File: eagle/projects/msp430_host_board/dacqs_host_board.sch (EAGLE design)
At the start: 167 parts, among them J1 MOL-SL-4-RA, J10 MOL-SL-3-V, J13 JST-PH-2TH-RA, J14 USB_MICROB_RECPT, J16 MOL-SL-2-RA, J17 CLM-112-02-L-D-IMU-MOUNT_IMU, J18 MOLSL-7-RA, J2 MOL-SL-4-RA, J3 MOL-SL-4-RA, J4 MOL-SL-4-RA, J5 MOL-SL-5-RA, J6 MOL-SL-3-V, J7 MOL-SL-5-V, J8 MOL-SL-3-RA, J9 MOL-SL-4-RA, U1 MSP430FR4994, U10 LSM9DS1, U2 MSP430FR4994, U3 PCT2075D,118, U4 MS560702BA03-50, U5 TPS61240DRVR, U6 LP5907_DBV_5, U7 MCP73831T, U8 INA219AIDCNR, U9 STD12NF06LT4, Y1 32.768kHz, Y2 4MHz, Y3 32.768kHz, Y4 4MHz

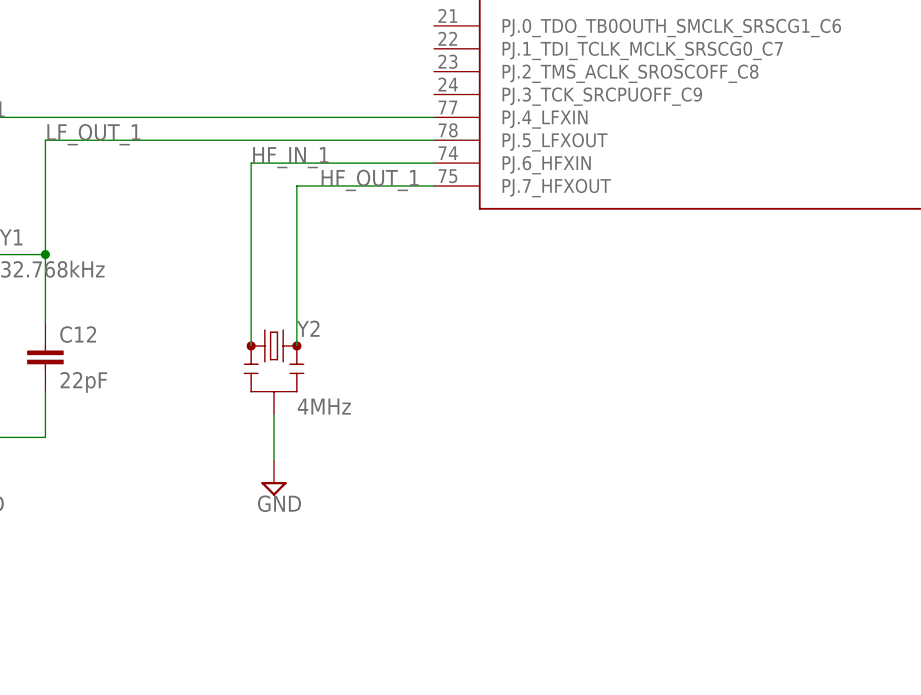
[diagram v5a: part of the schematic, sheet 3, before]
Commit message: Added 24Mhz oscillator for MSP430s
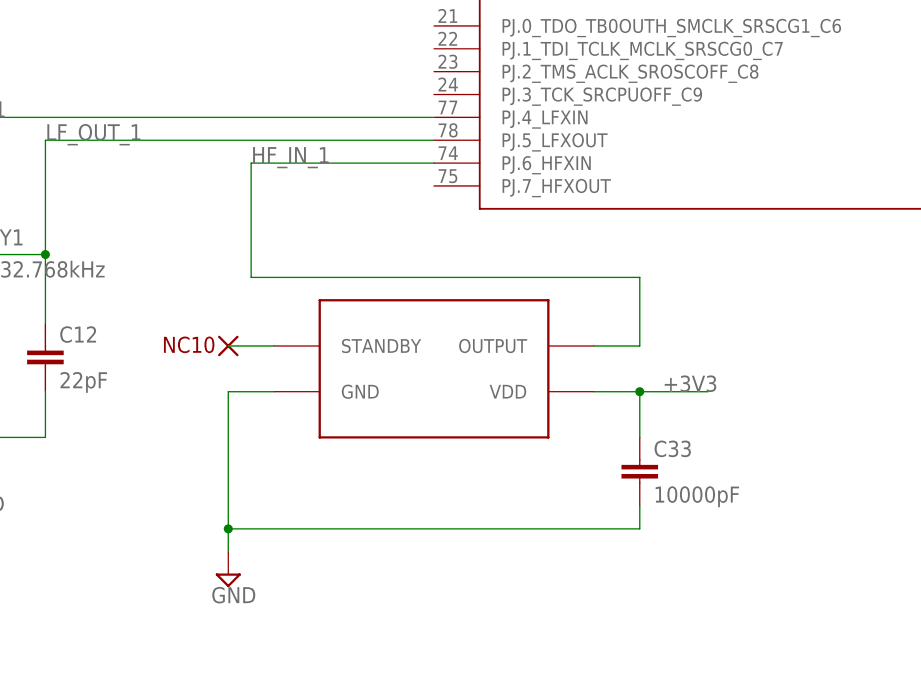
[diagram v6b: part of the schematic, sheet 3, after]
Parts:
- removed Y2, Y4: 4MHz, daqcs_host:RESONATOR4MHZ
- added C33, C34: 10000pF, daqcs_host:CAP_10000PF0_0603
- added NC10, NC11: NC, daqcs_host:NO_CONNECT
- added U$4, U$5: ASEMB-24MHZ-XY-T, daqcs_host:ASEMB-24MHZ-XY-T
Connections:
- removed net HF_OUT_1: U1.PJ.7_HFXOUT, Y2.3
- removed net HF_OUT_2: U2.PJ.7_HFXOUT, Y4.3
- new net N$4: NC10.NC, U$4.STANDBY
- new net N$5: NC11.NC, U$5.STANDBY
- net +3V3: now also C33.1, C34.1, U$4.VDD, U$5.VDD
- net GND: now also C33.2, C34.2, U$4.GND, U$5.GND; no longer Y2.2, Y4.2
- net HF_IN_1: now also U$4.OUTPUT; no longer Y2.1
- net HF_IN_2: now also U$5.OUTPUT; no longer Y4.1
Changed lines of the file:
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@@
 <part name="SUPPLY2" library="supply2" deviceset="GND" device=""/>
 <part name="Y1" library="daqcs_host" deviceset="CRYSTAL" device="3.2X1.5MM" value="32.768kHz"/>
-<part name="Y2" library="daqcs_host" deviceset="RESONATOR" device="4MHZ" value="4MHz"/>
 <part name="C11" library="daqcs_host" deviceset="CAP" device="_0603" technology="_22PF0" value="22pF"/>
 <part name="C12" library="daqcs_host" deviceset="CAP" device="_0603" technology="_22PF0" value="22pF"/>
@@
 <part name="SUPPLY4" library="supply2" deviceset="GND" device=""/>
 <part name="Y3" library="daqcs_host" deviceset="CRYSTAL" device="3.2X1.5MM" value="32.768kHz"/>
-<part name="Y4" library="daqcs_host" deviceset="RESONATOR" device="4MHZ" value="4MHz"/>
 <part name="C13" library="daqcs_host" deviceset="CAP" device="_0603" technology="_22PF0" value="22pF"/>
 <part name="C14" library="daqcs_host" deviceset="CAP" device="_0603" technology="_22PF0" value="22pF"/>
@@
 <part name="TP38" library="daqcs_host" deviceset="TEST_POINT" device="_10R_SMD" technology="_TP10R_SMD"/>
 <part name="U9" library="daqcs_host" deviceset="STD12NF06LT4" device=""/>
+<part name="U$4" library="daqcs_host" deviceset="ASEMB-24MHZ-XY-T" device=""/>
+<part name="NC10" library="daqcs_host" deviceset="NO_CONNECT" device="" value="NC"/>
+<part name="C33" library="daqcs_host" deviceset="CAP" device="_0603" technology="_10000PF0" value="10000pF"/>
+<part name="U$5" library="daqcs_host" deviceset="ASEMB-24MHZ-XY-T" device=""/>
+<part name="NC11" library="daqcs_host" deviceset="NO_CONNECT" device="" value="NC"/>
+<part name="C34" library="daqcs_host" deviceset="CAP" device="_0603" technology="_10000PF0" value="10000pF"/>
 </parts>
 <sheets>
@@
 <instance part="SUPPLY1" gate="GND" x="251.46" y="55.88"/>
 <instance part="Y1" gate="G$1" x="5.08" y="55.88"/>
-<instance part="Y2" gate="G$1" x="38.1" y="45.72"/>
 <instance part="C11" gate="G$1" x="-2.54" y="43.18"/>
 <instance part="C12" gate="G$1" x="12.7" y="43.18"/>
 <instance part="SUPPLY3" gate="GND" x="5.08" y="30.48"/>
-<instance part="SUPPLY4" gate="GND" x="38.1" y="30.48"/>
+<instance part="SUPPLY4" gate="GND" x="33.02" y="20.32"/>
 <instance part="DS4" gate="G$1" x="-15.24" y="172.72" rot="R270"/>
 <instance part="DS5" gate="G$1" x="-15.24" y="160.02" rot="R270"/>
@@
 <instance part="R27" gate="G$1" x="7.62" y="160.02"/>
 <instance part="SUPPLY31" gate="GND" x="-25.4" y="149.86"/>
+<instance part="U$4" gate="G$1" x="55.88" y="43.18"/>
+<instance part="NC10" gate="G$1" x="33.02" y="45.72"/>
+<instance part="C33" gate="G$1" x="78.74" y="30.48"/>
 </instances>
 <busses>
@@
 <junction x="271.78" y="78.74"/>
 <pinref part="+3V2" gate="G$1" pin="+3V3"/>
+</segment>
+<segment>
+<pinref part="U$4" gate="G$1" pin="VDD"/>
+<wire x1="73.66" y1="40.64" x2="78.74" y2="40.64" width="0.1524" layer="91"/>
+<label x="81.28" y="40.64" size="1.778" layer="95"/>
+<pinref part="C33" gate="G$1" pin="1"/>
+<wire x1="78.74" y1="40.64" x2="86.36" y2="40.64" width="0.1524" layer="91"/>
+<wire x1="78.74" y1="40.64" x2="78.74" y2="35.56" width="0.1524" layer="91"/>
+<junction x="78.74" y="40.64"/>
 </segment>
 </net>
@@
 </segment>
 <segment>
-<pinref part="Y2" gate="G$1" pin="2"/>
 <pinref part="SUPPLY4" gate="GND" pin="GND"/>
-<wire x1="38.1" y1="38.1" x2="38.1" y2="33.02" width="0.1524" layer="91"/>
+<wire x1="33.02" y1="40.64" x2="33.02" y2="25.4" width="0.1524" layer="91"/>
+<pinref part="U$4" gate="G$1" pin="GND"/>
+<wire x1="33.02" y1="25.4" x2="33.02" y2="22.86" width="0.1524" layer="91"/>
+<wire x1="38.1" y1="40.64" x2="33.02" y2="40.64" width="0.1524" layer="91"/>
+<pinref part="C33" gate="G$1" pin="2"/>
+<wire x1="78.74" y1="27.94" x2="78.74" y2="25.4" width="0.1524" layer="91"/>
+<wire x1="78.74" y1="25.4" x2="33.02" y2="25.4" width="0.1524" layer="91"/>
+<junction x="33.02" y="25.4"/>
 </segment>
 <segment>
@@
 </segment>
 </net>
-<net name="HF_OUT_1" class="0">
-<segment>
-<pinref part="U1" gate="A" pin="PJ.7_HFXOUT"/>
-<pinref part="Y2" gate="G$1" pin="3"/>
-<wire x1="55.88" y1="63.5" x2="40.64" y2="63.5" width="0.1524" layer="91"/>
-<wire x1="40.64" y1="63.5" x2="40.64" y2="45.72" width="0.1524" layer="91"/>
-<label x="43.18" y="63.5" size="1.778" layer="95"/>
-</segment>
-</net>
 <net name="HF_IN_1" class="0">
 <segment>
-<pinref part="Y2" gate="G$1" pin="1"/>
-<wire x1="35.56" y1="45.72" x2="35.56" y2="66.04" width="0.1524" layer="91"/>
 <pinref part="U1" gate="A" pin="PJ.6_HFXIN"/>
 <wire x1="35.56" y1="66.04" x2="55.88" y2="66.04" width="0.1524" layer="91"/>
 <label x="35.56" y="66.04" size="1.778" layer="95"/>
+<pinref part="U$4" gate="G$1" pin="OUTPUT"/>
+<wire x1="73.66" y1="45.72" x2="78.74" y2="45.72" width="0.1524" layer="91"/>
+<wire x1="78.74" y1="45.72" x2="78.74" y2="53.34" width="0.1524" layer="91"/>
+<wire x1="78.74" y1="53.34" x2="35.56" y2="53.34" width="0.1524" layer="91"/>
+<wire x1="35.56" y1="53.34" x2="35.56" y2="66.04" width="0.1524" layer="91"/>
 </segment>
 </net>
@@
 <wire x1="2.54" y1="172.72" x2="-12.7" y2="172.72" width="0.1524" layer="91"/>
 <label x="-12.7" y="172.72" size="1.778" layer="95"/>
+</segment>
+</net>
+<net name="N$4" class="0">
+<segment>
+<pinref part="NC10" gate="G$1" pin="NC"/>
+<pinref part="U$4" gate="G$1" pin="STANDBY"/>
+<wire x1="33.02" y1="45.72" x2="38.1" y2="45.72" width="0.1524" layer="91"/>
 </segment>
 </net>
@@
 <instance part="SUPPLY2" gate="GND" x="289.56" y="60.96"/>
 <instance part="Y3" gate="G$1" x="40.64" y="58.42"/>
-<instance part="Y4" gate="G$1" x="76.2" y="50.8"/>
 <instance part="C13" gate="G$1" x="33.02" y="45.72"/>
 <instance part="C14" gate="G$1" x="50.8" y="45.72"/>
 <instance part="SUPPLY5" gate="GND" x="40.64" y="33.02"/>
-<instance part="SUPPLY6" gate="GND" x="76.2" y="33.02"/>
+<instance part="SUPPLY6" gate="GND" x="73.66" y="25.4"/>
 <instance part="R4" gate="G$1" x="-12.7" y="175.26" smashed="yes" rot="R90">
 <attribute name="NAME" x="-14.1986" y="176.53" size="1.778" layer="95" rot="R180"/>
@@
 </instance>
 <instance part="DS7" gate="G$1" x="20.32" y="170.18" rot="R270"/>
+<instance part="U$5" gate="G$1" x="96.52" y="48.26"/>
+<instance part="NC11" gate="G$1" x="73.66" y="50.8"/>
+<instance part="C34" gate="G$1" x="116.84" y="38.1"/>
 </instances>
 <busses>
@@
 <wire x1="40.64" y1="149.86" x2="40.64" y2="147.32" width="0.1524" layer="91"/>
 <junction x="33.02" y="149.86"/>
+</segment>
+<segment>
+<pinref part="U$5" gate="G$1" pin="VDD"/>
+<wire x1="114.3" y1="45.72" x2="116.84" y2="45.72" width="0.1524" layer="91"/>
+<pinref part="C34" gate="G$1" pin="1"/>
+<wire x1="116.84" y1="45.72" x2="129.54" y2="45.72" width="0.1524" layer="91"/>
+<wire x1="116.84" y1="45.72" x2="116.84" y2="43.18" width="0.1524" layer="91"/>
+<junction x="116.84" y="45.72"/>
+<label x="121.92" y="45.72" size="1.778" layer="95"/>
 </segment>
 </net>
@@
 </segment>
 <segment>
-<pinref part="Y4" gate="G$1" pin="2"/>
 <pinref part="SUPPLY6" gate="GND" pin="GND"/>
-<wire x1="76.2" y1="43.18" x2="76.2" y2="35.56" width="0.1524" layer="91"/>
+<wire x1="73.66" y1="45.72" x2="73.66" y2="33.02" width="0.1524" layer="91"/>
+<pinref part="U$5" gate="G$1" pin="GND"/>
+<wire x1="73.66" y1="33.02" x2="73.66" y2="27.94" width="0.1524" layer="91"/>
+<wire x1="78.74" y1="45.72" x2="73.66" y2="45.72" width="0.1524" layer="91"/>
+<pinref part="C34" gate="G$1" pin="2"/>
+<wire x1="116.84" y1="35.56" x2="116.84" y2="33.02" width="0.1524" layer="91"/>
+<wire x1="116.84" y1="33.02" x2="73.66" y2="33.02" width="0.1524" layer="91"/>
+<junction x="73.66" y="33.02"/>
 </segment>
 <segment>
@@
 <net name="HF_IN_2" class="0">
 <segment>
-<pinref part="Y4" gate="G$1" pin="1"/>
-<wire x1="73.66" y1="50.8" x2="73.66" y2="71.12" width="0.1524" layer="91"/>
 <pinref part="U2" gate="A" pin="PJ.6_HFXIN"/>
 <wire x1="73.66" y1="71.12" x2="91.44" y2="71.12" width="0.1524" layer="91"/>
 <label x="73.66" y="71.12" size="1.778" layer="95"/>
-</segment>
-</net>
-<net name="HF_OUT_2" class="0">
-<segment>
-<pinref part="U2" gate="A" pin="PJ.7_HFXOUT"/>
-<pinref part="Y4" gate="G$1" pin="3"/>
-<wire x1="91.44" y1="68.58" x2="78.74" y2="68.58" width="0.1524" layer="91"/>
-<wire x1="78.74" y1="68.58" x2="78.74" y2="50.8" width="0.1524" layer="91"/>
-<label x="78.74" y="68.58" size="1.778" layer="95"/>
+<pinref part="U$5" gate="G$1" pin="OUTPUT"/>
+<wire x1="114.3" y1="50.8" x2="116.84" y2="50.8" width="0.1524" layer="91"/>
+<wire x1="116.84" y1="50.8" x2="116.84" y2="60.96" width="0.1524" layer="91"/>
+<wire x1="116.84" y1="60.96" x2="73.66" y2="60.96" width="0.1524" layer="91"/>
+<wire x1="73.66" y1="60.96" x2="73.66" y2="71.12" width="0.1524" layer="91"/>
 </segment>
 </net>
@@
 </segment>
 </net>
+<net name="N$5" class="0">
+<segment>
+<pinref part="NC11" gate="G$1" pin="NC"/>
+<pinref part="U$5" gate="G$1" pin="STANDBY"/>
+<wire x1="73.66" y1="50.8" x2="78.74" y2="50.8" width="0.1524" layer="91"/>
+</segment>
+</net>

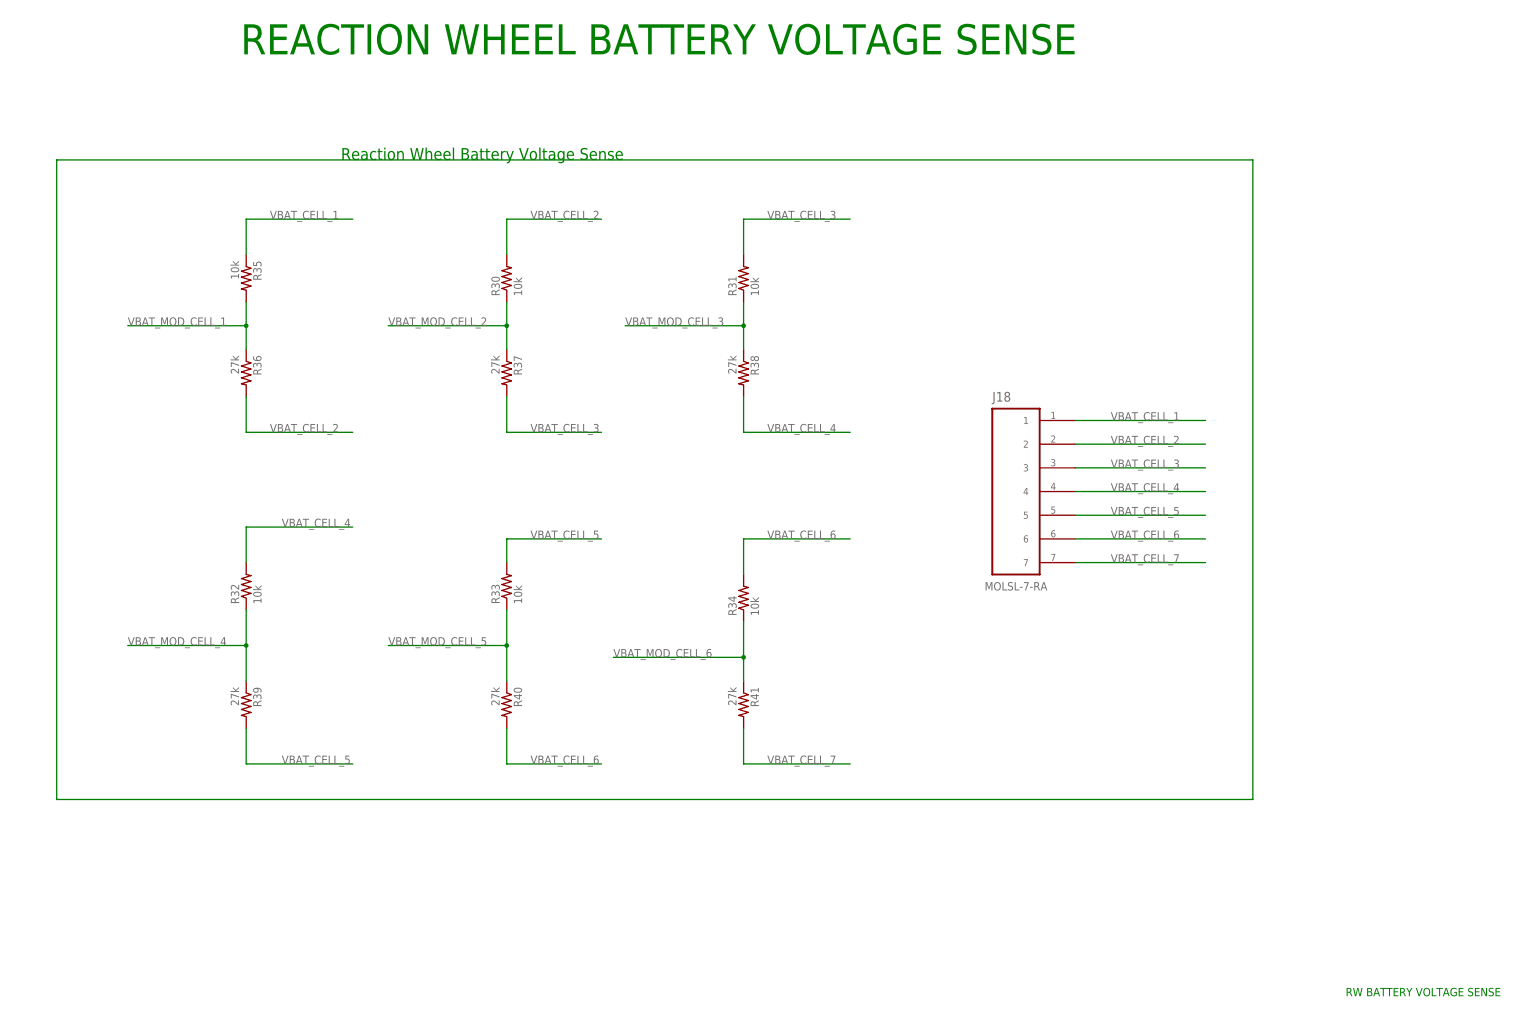
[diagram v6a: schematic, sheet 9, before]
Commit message: Added headers for both MSP430s to pin out the additonal GPIO
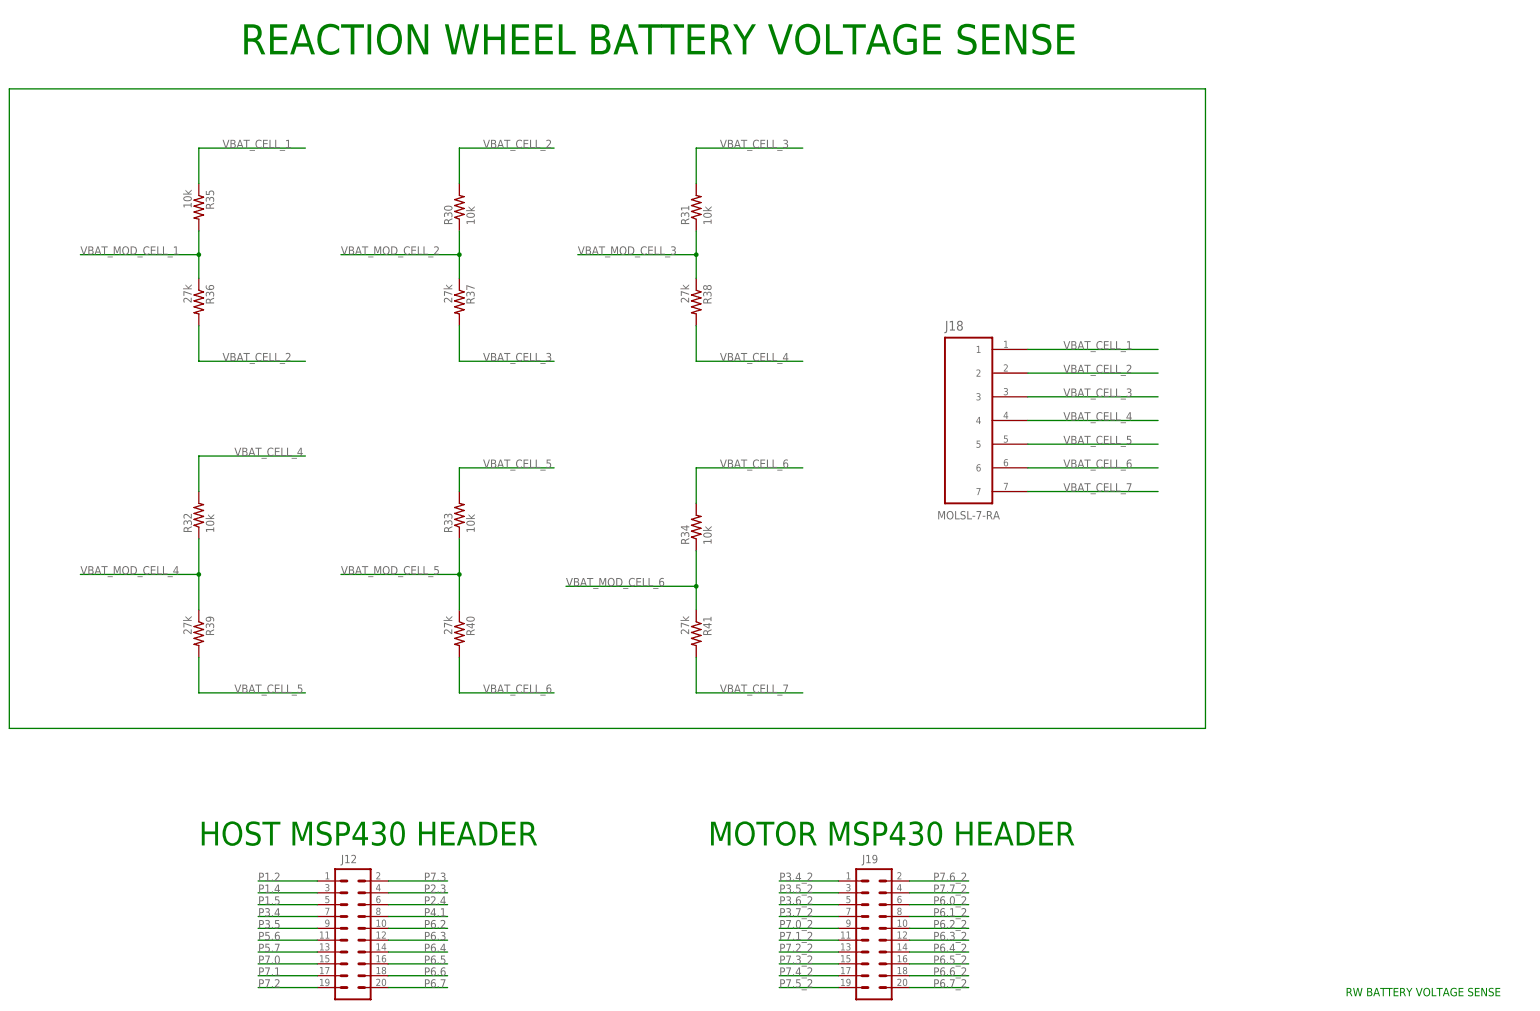
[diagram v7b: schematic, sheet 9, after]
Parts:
- added J12, J19: (no value), daqcs_host:M10X2
- added NC12, NC13, NC14, NC15, NC16, NC17, NC18, NC19, NC20, NC21, NC22, NC23, NC24, NC25, NC26, NC27, NC28, NC29, NC30, NC31, NC32, NC33, NC34, NC35, NC36, NC37, NC38, NC39, NC40, NC41, NC42, NC43, NC44, NC45, NC46, NC47, NC48, NC49, NC50, NC51, NC52, NC53: NC, daqcs_host:NO_CONNECT
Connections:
- new net N$10: NC12.NC, U1.P3.3_A15_C15
- new net N$11: NC13.NC, U1.P3.6_TB0.5
- new net N$12: NC14.NC, U1.P3.7_TB0.6
- new net N$13: NC15.NC, U1.PJ.0_TDO_TB0OUTH_SMCLK_SRSCG1_C6
- new net N$14: NC16.NC, U1.PJ.1_TDI_TCLK_MCLK_SRSCG0_C7
- new net N$15: NC17.NC, U1.PJ.2_TMS_ACLK_SROSCOFF_C8
- new net N$16: NC18.NC, U1.PJ.3_TCK_SRCPUOFF_C9
- new net N$17: NC19.NC, U1.PJ.7_HFXOUT
- new net N$18: NC20.NC, U1.P2.7
- new net N$19: NC21.NC, U1.P4.2_A10
- new net N$20: NC22.NC, U1.P4.3_A11
- new net N$21: NC36.NC, U2.P3.3_A15_C15
- new net N$24: NC23.NC, U2.P5.2_UCB1CLK_TA4CLK
- new net N$25: NC24.NC, U2.P5.3_UCB1STE
- new net N$26: NC25.NC, U2.PJ.0_TDO_TB0OUTH_SMCLK_SRSCG1_C6
- new net N$31: NC26.NC, U2.PJ.1_TDI_TCLK_MCLK_SRSCG0_C7
- new net N$32: NC27.NC, U2.PJ.2_TMS_ACLK_SROSCOFF_C8
- new net N$33: NC28.NC, U2.PJ.3_TCK_SRCPUOFF_C9
- new net N$34: NC29.NC, U2.PJ.7_HFXOUT
- new net N$35: NC30.NC, U2.P2.2_TB0.2_UCB0CLK
- new net N$36: NC31.NC, U2.P4.3_A11
- new net N$38: NC32.NC, U2.P4.4_TB0.5
- new net N$39: NC33.NC, U2.P4.5
- new net N$40: NC34.NC, U2.P4.6
- new net N$41: NC35.NC, U2.P4.7
- new net N$42: NC37.NC, U5.EP
- new net N$43: NC38.NC, U6.NC
- new net N$44: J14.D-, NC39.NC
- new net N$45: J14.D+, NC40.NC
- new net N$46: J14.ID, NC41.NC
- new net N$47: J17.7, NC42.NC
- new net N$48: J17.9, NC43.NC
- new net N$49: J17.17, NC44.NC
- new net N$50: J17.19, NC45.NC
- new net N$51: J17.21, NC46.NC
- new net N$52: J17.23, NC47.NC
- new net N$53: J17.2, NC48.NC
- new net N$54: J17.16, NC49.NC
- new net N$55: J17.18, NC50.NC
- new net N$56: J17.20, NC51.NC
- new net N$57: J17.22, NC52.NC
- new net N$58: J17.24, NC53.NC
- new net P1.2: J12.1, U1.P1.2_TA1.1_TA0CLK_COUT_A2_C2
- new net P1.4: J12.3, U1.P1.4_TB0.1_UCA0STE_A4_C4
- new net P1.5: J12.5, U1.P1.5_TB0.2_UCA0CLK_A5_C5
- new net P2.3: J12.4, U1.P2.3_TA0.0_UCA1STE_A6_C10
- new net P2.4: J12.6, U1.P2.4_TA1.0_UCA1CLK_A7_C11
- new net P3.4: J12.7, U1.P3.4_TB0.3_SMCLK
- new net P3.4_2: J19.1, U2.P3.4_TB0.3_SMCLK
- new net P3.5: J12.9, U1.P3.5_TB0.4_COUT
- new net P3.5_2: J19.3, U2.P3.5_TB0.4_COUT
- new net P3.6_2: J19.5, U2.P3.6_TB0.5
- new net P3.7_2: J19.7, U2.P3.7_TB0.6
- new net P4.1: J12.8, U1.P4.1_A9
- new net P5.6: J12.11, U1.P5.6_UCA2CLK_TA4.0_SMCLK
- new net P5.7: J12.13, U1.P5.7_UCA2STE_TA4.1_MCLK
- new net P6.0_2: J19.6, U2.P6.0_UCA3TXD_UCA3SIMO
- new net P6.1_2: J19.8, U2.P6.1_UCA3RXD_UCA3SOMI
- new net P6.2: J12.10, U1.P6.2_UCA3CLK
- new net P6.2_2: J19.10, U2.P6.2_UCA3CLK
- new net P6.3: J12.12, U1.P6.3_UCA3STE
- new net P6.3_2: J19.12, U2.P6.3_UCA3STE
- new net P6.4: J12.14, U1.P6.4_UCB3SIMO_UCB3SDA
- new net P6.4_2: J19.14, U2.P6.4_UCB3SIMO_UCB3SDA
- new net P6.5: J12.16, U1.P6.5_UCB3SOMI_UCB3SCL
- new net P6.5_2: J19.16, U2.P6.5_UCB3SOMI_UCB3SCL
- new net P6.6: J12.18, U1.P6.6_UCB3CLK
- new net P6.6_2: J19.18, U2.P6.6_UCB3CLK
- new net P6.7: J12.20, U1.P6.7_UCB3STE
- new net P6.7_2: J19.20, U2.P6.7_UCB3STE
- new net P7.0: J12.15, U1.P7.0_UCB2SIMO_UCB2SDA
- new net P7.0_2: J19.9, U2.P7.0_UCB2SIMO_UCB2SDA
- new net P7.1: J12.17, U1.P7.1_UCB2SOMI_UCB2SCL
- new net P7.1_2: J19.11, U2.P7.1_UCB2SOMI_UCB2SCL
- new net P7.2: J12.19, U1.P7.2_UCB2CLK
- new net P7.2_2: J19.13, U2.P7.2_UCB2CLK
- new net P7.3: J12.2, U1.P7.3_UCB2STE_TA4.1
- new net P7.3_2: J19.15, U2.P7.3_UCB2STE_TA4.1
- new net P7.4_2: J19.17, U2.P7.4__TA4.0_A16
- new net P7.5_2: J19.19, U2.P7.5_A17
- new net P7.6_2: J19.2, U2.P7.6_A18
- new net P7.7_2: J19.4, U2.P7.7_A19
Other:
- note added: "HOST MSP430 HEADER"
- note added: "MOTOR MSP430 HEADER"
- note removed: "Reaction Wheel Battery Voltage Sense"
- moved on the sheet: J18, R30, R31, R32, R33, R34, R35, R36, R37, R38, R39, R40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
